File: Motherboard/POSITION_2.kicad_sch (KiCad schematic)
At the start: 27 parts, among them Q10 MOSFET_N_(DMN61D8LQ-13), Q8 MOSFET_N_(ZVN3320FTA)

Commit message: Schematic ready.  Going to clean up directory now.
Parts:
- C23, C27, C28, C29, C30: footprint Capacitors_SMD:C_1206 -> Capacitor_SMD:C_1206_3216Metric
- CAL3, CAL4: footprint (none) -> Smart_Tank:FEMALE_SPADE_QC_(TE_63969-1)
- CTRL_SHUNT_2, PUMP_SHUNT_2: footprint _GARRETTS_PARTS:SHUNT_(WSL40261L000FEA) -> Smart_Tank:SHUNT_(WSL40261L000FEA)
- D3, D6: footprint Diodes_SMD:SOD-123 -> Diode_SMD:D_SMA
- Q8: footprint TO_SOT_Packages_SMD:SOT-23 -> Package_TO_SOT_SMD:SOT-23
- R49, R52, R55, R56, R57, R8: footprint Resistors_SMD:R_1206 -> Resistor_SMD:R_1206_3216Metric
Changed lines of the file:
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@@
 			)
 		)
-		(property "Footprint" "Resistors_SMD:R_1206"
+		(property "Footprint" "Resistor_SMD:R_1206_3216Metric"
 			(at 184.658 86.36 90)
 			(effects
@@
 			)
 		)
-		(property "Footprint" "Resistors_SMD:R_1206"
+		(property "Footprint" "Resistor_SMD:R_1206_3216Metric"
 			(at 116.078 81.28 90)
 			(effects
@@
 			)
 		)
-		(property "Footprint" "Resistors_SMD:R_1206"
+		(property "Footprint" "Resistor_SMD:R_1206_3216Metric"
 			(at 100.33 92.202 90)
 			(effects
@@
 			)
 		)
-		(property "Footprint" "_GARRETTS_PARTS:SHUNT_(WSL40261L000FEA)"
+		(property "Footprint" "Smart_Tank:SHUNT_(WSL40261L000FEA)"
 			(at 194.31 53.848 90)
 			(effects
@@
 			)
 		)
-		(property "Footprint" "Capacitors_SMD:C_1206"
+		(property "Footprint" "Capacitor_SMD:C_1206_3216Metric"
 			(at 228.2952 53.34 0)
 			(effects
@@
 			)
 		)
-		(property "Footprint" "TO_SOT_Packages_SMD:SOT-23"
+		(property "Footprint" "Package_TO_SOT_SMD:SOT-23"
 			(at 118.11 94.615 0)
 			(effects
@@
 			)
 		)
-		(property "Footprint" "Capacitors_SMD:C_1206"
+		(property "Footprint" "Capacitor_SMD:C_1206_3216Metric"
 			(at 218.1352 53.34 0)
 			(effects
@@
 			)
 		)
-		(property "Footprint" ""
+		(property "Footprint" "Smart_Tank:FEMALE_SPADE_QC_(TE_63969-1)"
 			(at 194.31 107.95 0)
 			(effects
@@
 			)
 		)
-		(property "Footprint" "Resistors_SMD:R_1206"
+		(property "Footprint" "Resistor_SMD:R_1206_3216Metric"
 			(at 93.218 99.06 90)
 			(effects
@@
 			)
 		)
-		(property "Footprint" "Resistors_SMD:R_1206"
+		(property "Footprint" "Resistor_SMD:R_1206_3216Metric"
 			(at 72.898 43.18 90)
 			(effects
@@
 			)
 		)
-		(property "Footprint" "Capacitors_SMD:C_1206"
+		(property "Footprint" "Capacitor_SMD:C_1206_3216Metric"
 			(at 218.1352 139.7 0)
 			(effects
@@
 			)
 		)
-		(property "Footprint" "Capacitors_SMD:C_1206"
+		(property "Footprint" "Capacitor_SMD:C_1206_3216Metric"
 			(at 256.54 48.5648 0)
 			(effects
@@
 			)
 		)
-		(property "Footprint" "Diodes_SMD:SOD-123"
+		(property "Footprint" "Diode_SMD:D_SMA"
 			(at 236.22 80.01 0)
 			(effects
@@
 			)
 		)
-		(property "Footprint" "_GARRETTS_PARTS:SHUNT_(WSL40261L000FEA)"
+		(property "Footprint" "Smart_Tank:SHUNT_(WSL40261L000FEA)"
 			(at 194.31 140.208 90)
 			(effects
@@
 			)
 		)
-		(property "Footprint" ""
+		(property "Footprint" "Smart_Tank:FEMALE_SPADE_QC_(TE_63969-1)"
 			(at 252.73 33.02 0)
 			(effects
@@
 			)
 		)
-		(property "Footprint" "Capacitors_SMD:C_1206"
+		(property "Footprint" "Capacitor_SMD:C_1206_3216Metric"
 			(at 228.2952 139.7 0)
 			(effects
@@
 			)
 		)
-		(property "Footprint" "Diodes_SMD:SOD-123"
+		(property "Footprint" "Diode_SMD:D_SMA"
 			(at 252.73 41.91 0)
 			(effects
@@
 			)
 		)
-		(property "Footprint" "Resistors_SMD:R_1206"
+		(property "Footprint" "Resistor_SMD:R_1206_3216Metric"
 			(at 189.23 78.232 90)
 			(effects

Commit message: Started cleaning out old parts from PCB.
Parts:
- PUMP_V_CONN_2: footprint Smart_Tank:PHNX_TB_SCREW_4_POS_(1729144) -> Smart_Tank:PHX_TB_HDR_4_POS_STR_(1755752)
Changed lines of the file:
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@@
 			)
 		)
-		(property "Footprint" "Smart_Tank:PHNX_TB_SCREW_4_POS_(1729144)"
+		(property "Footprint" "Smart_Tank:PHX_TB_HDR_4_POS_STR_(1755752)"
 			(at 248.92 83.82 0)
 			(effects

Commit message: Almost done with re-routing.
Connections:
- net POS_2_SPARE renamed POS_2_SPR_1
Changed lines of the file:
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@@
 		)
 	)
-	(global_label "POS_2_SPARE"
+	(global_label "POS_2_SPR_1"
 		(shape input)
 		(at 57.15 59.69 0)

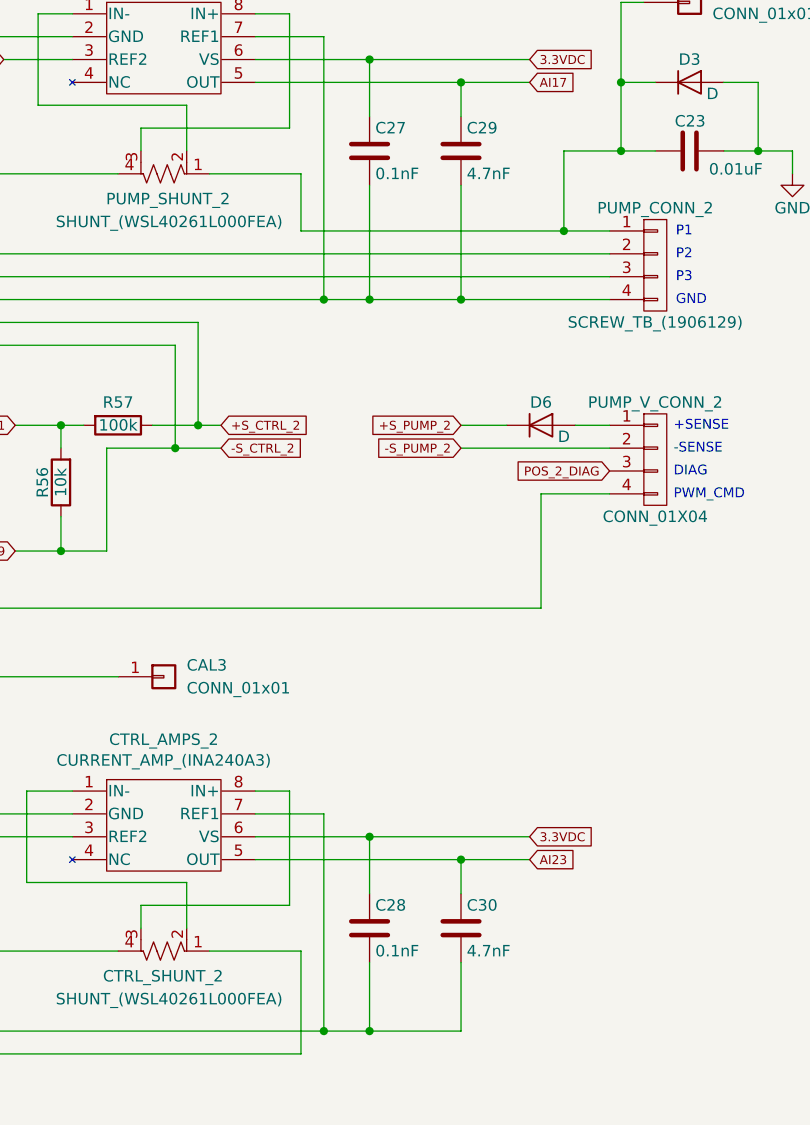
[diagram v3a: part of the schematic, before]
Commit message: Capacitor part issues...
Made these changes...

Concerning C13, C15, C27, C28, C31, C32, C35, C36, C39, C40, C43, C44
The schematic is wrong, and the BOM is correct.  These should all be 0.1uF
Concerning C20, C21, C29, C30, C33, C34, C37, C38, C41, C42, C45, C46
The BOM is wrong, and the schematic is correct.  These should all be 4.7nF
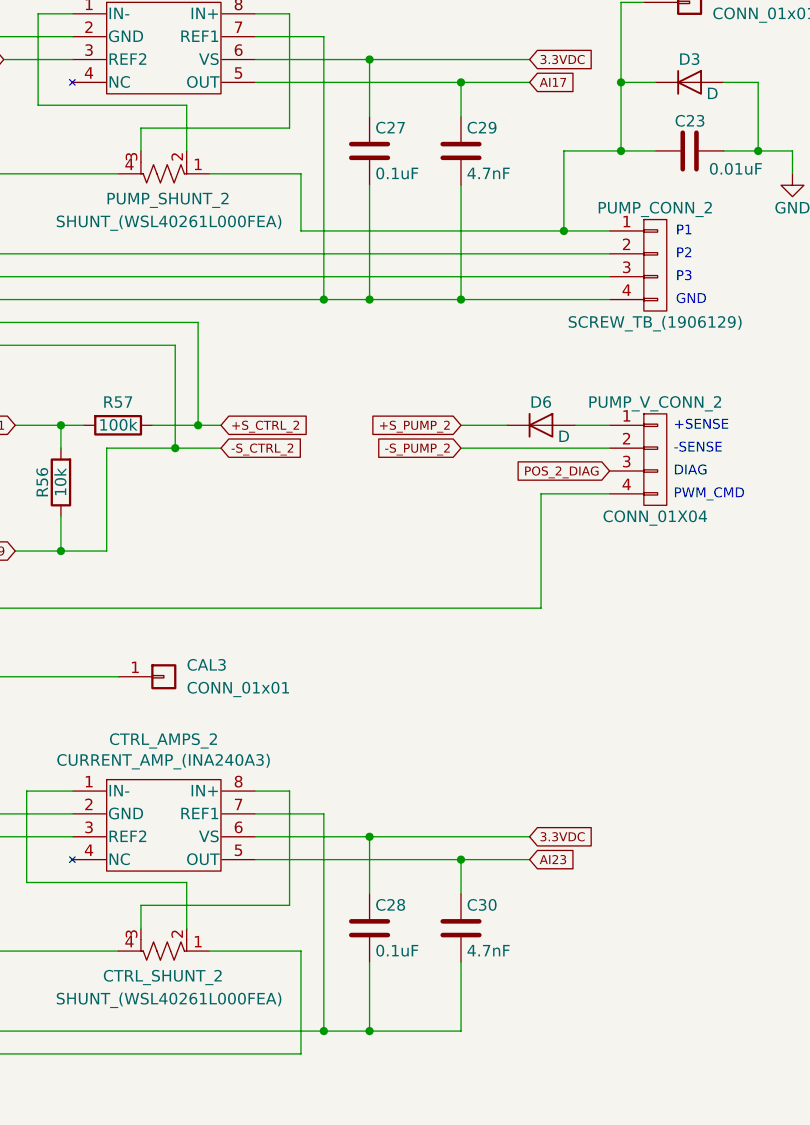
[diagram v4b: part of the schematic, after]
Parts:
- C27, C28: value 0.1nF -> 0.1uF
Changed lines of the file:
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@@
 			)
 		)
-		(property "Value" "0.1nF"
+		(property "Value" "0.1uF"
 			(at 217.805 52.07 0)
 			(effects
@@
 			)
 		)
-		(property "Value" "0.1nF"
+		(property "Value" "0.1uF"
 			(at 217.805 138.43 0)
 			(effects
